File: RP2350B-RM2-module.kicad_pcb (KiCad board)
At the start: 4 copper layers, 33.7 x 68.8 mm, 58 parts, among them J1 SM03B-SRSS-TB, J2 Conn_01x26_Socket, J3 Conn_01x26_Socket, J5 USB_C_Receptacle_USB2.0_16P, SW1 SW_Push, SW2 SW_Push, U1 W25Q128JWSIQ, U2 APS6404L-SQH-SN, U3 RP2350_80QFN, U4 RM2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

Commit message: clean ERC and DRC
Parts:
- U1: value W25Q128JWSIQ -> W25Q128JVSIQ
- U2: value APS6404L-SQH-SN -> APS6404L-3SQR-SN
- U4: value RM2 -> <value>
- moved C24 0.97 mm to (91.4, 93.9)
- moved C21 0.82 mm to (91.5, 96.5)
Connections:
- net /EN renamed /3V3_EN
- U3 pad 23: +3V3 -> /WL_ON
- U4 pad 12: +3V3 -> /WL_ON
- U4 pad 13: +3V3 -> /WL_ON
- U4 pad 14: unconnected-(U4-VDDIO-Pad14) -> +3V3
- U5 pad 2: unconnected-(U5-GND-Pad2) -> GND
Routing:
- net /WL_ON: track 0.00 -> 26.0 mm, vias 0 -> 2
- net +3V3: track 55.5 -> 56.8 mm

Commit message: Changed PSRAM
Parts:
- U2: value APS6404L-3SQR-SN -> APS6404L-3SQN-SN
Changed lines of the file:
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@@
 			)
 		)
-		(property "Value" "APS6404L-3SQR-SN"
+		(property "Value" "APS6404L-3SQN-SN"
 			(at 0 3.43 0)
 			(layer "F.Fab")

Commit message: Added ADC vref
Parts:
- added C25: 100n, Capacitor_SMD:C_0402_1005Metric, F.Cu at (105.3, 70.9)
- added C26: 100n, Capacitor_SMD:C_0402_1005Metric, F.Cu at (104.3, 71.9)
- added TP2: TestPoint_Square, TestPoint:TestPoint_Pad_1.5x1.5mm, B.Cu at (109.0, 48.0)
- added TP3: TestPoint, TestPoint:TestPoint_Pad_D1.5mm, F.Cu at (102.0, 64.2)
- added U6: MCP1501-30xCH, Package_TO_SOT_SMD:SOT-23-6, F.Cu at (105.9, 68.5)
- moved C19 1.27 mm to (102.7, 70.3), turned to 90 degrees
- moved C8 0.45 mm to (102.7, 68.5)
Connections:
- U3 pad 59: +3V3 -> /ADC_AVDD
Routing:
- net /RUN: track 16.5 -> 55.8 mm, vias 3 -> 6
- net /ADC_AVDD: track 0.00 -> 15.0 mm
- net /PSRAM_CS: track 39.5 -> 47.6 mm
- net GND: track 5.63 -> 8.18 mm, vias 55 -> 57
- net +3V3: track 56.8 -> 58.3 mm, vias 21 -> 22
- net /GPIO46_ADC6: track 21.5 -> 22.9 mm
- net /GPIO42_ADC2: track 13.2 -> 14.6 mm
- net /GPIO44_ADC4: track 17.4 -> 18.7 mm
- net /GPIO45_ADC5: track 19.5 -> 20.8 mm
- net /GPIO43_ADC3: track 15.4 -> 16.6 mm
- net /GPIO41_ADC1: track 12.3 -> 12.9 mm
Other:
- board text added: "1"
- board text added: "IAN ARCHBELL"
- board text added: "MIT LIC."

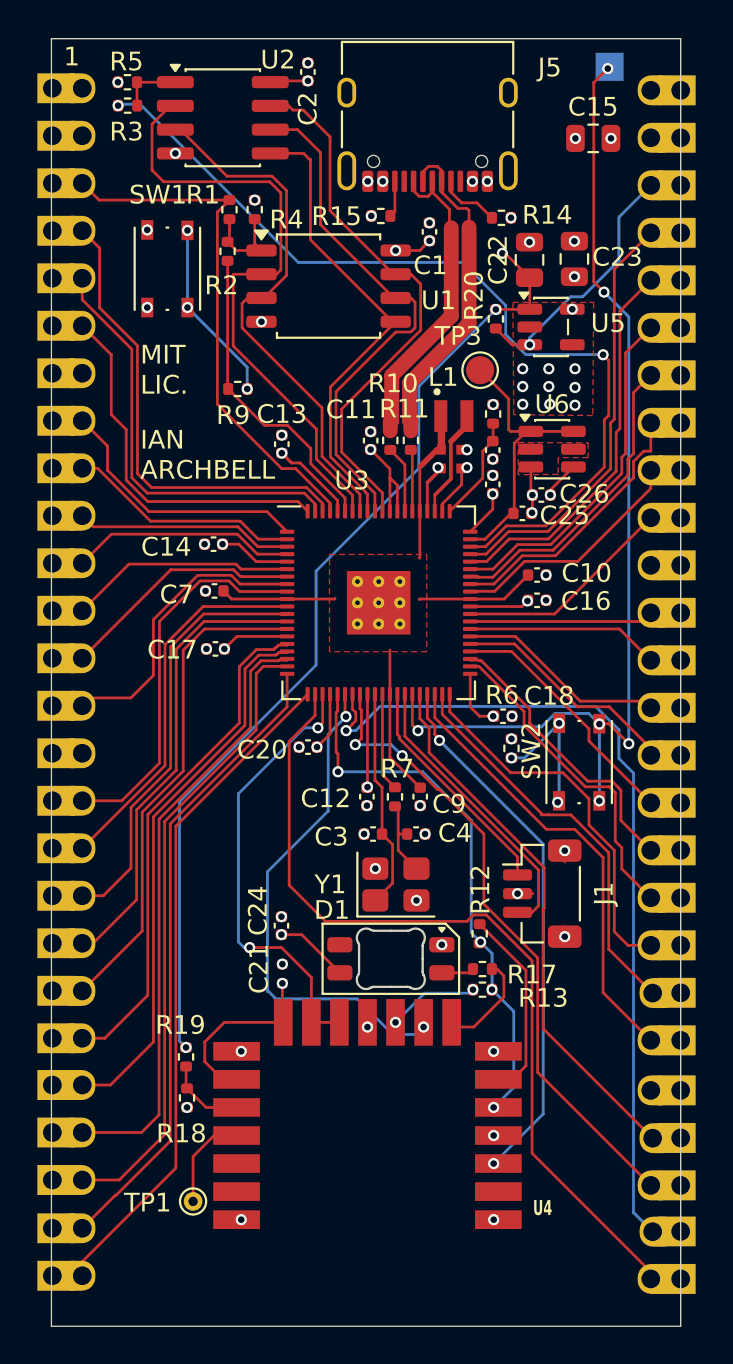
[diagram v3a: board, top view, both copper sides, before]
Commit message: Added pin numbering
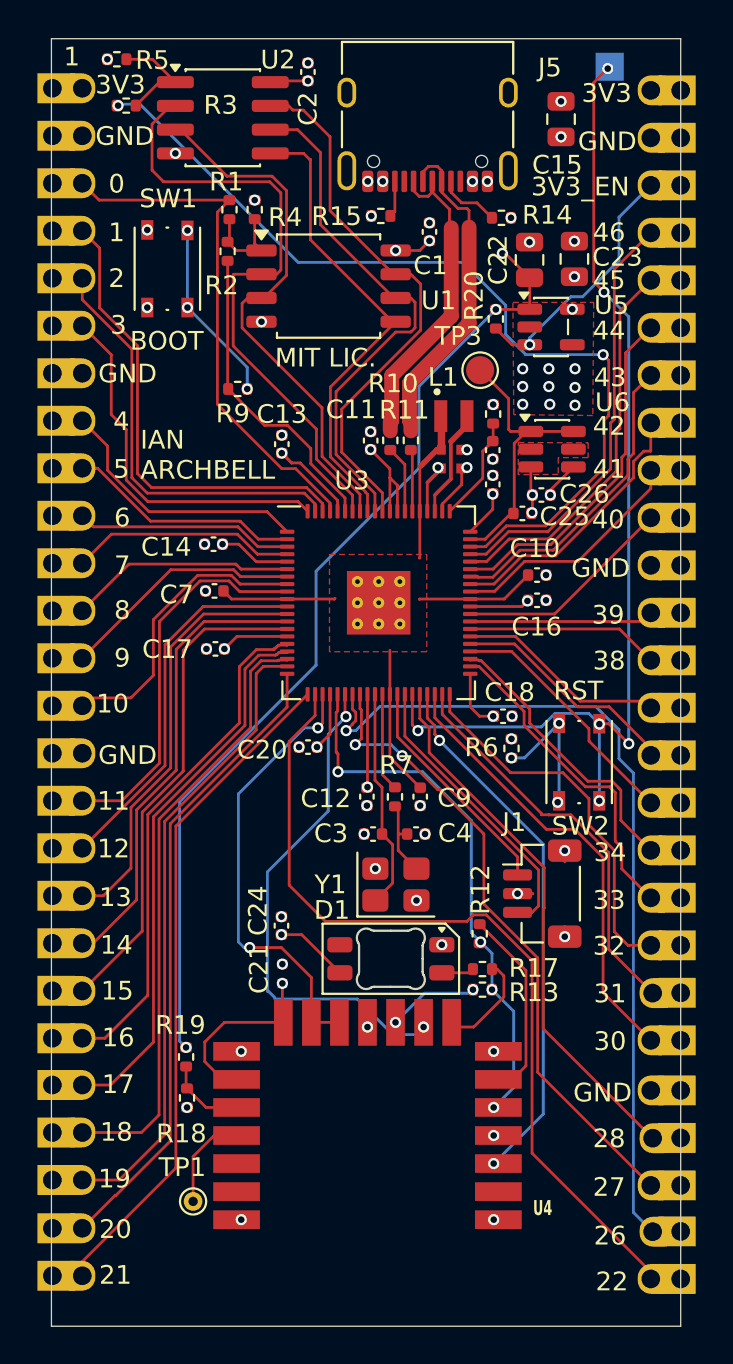
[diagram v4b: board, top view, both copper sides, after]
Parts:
- moved C15 2.00 mm to (106.3, 50.8), turned to -90 degrees
- moved R5 1.35 mm to (82.6, 47.6)
- moved R3 0.08 mm to (83.1, 50.1)
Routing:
- net /FLASH2_SS: track 3.31 -> 5.76 mm
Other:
- board text added: "0"
- board text added: "10"
- board text added: "11"
- board text added: "12"
- board text added: "13"
- board text added: "14"
- board text added: "15"
- board text added: "16"
- board text added: "17"
- board text added: "18"
- board text added: "19"
- board text added: "2"
- board text added: "20"
- board text added: "21"
- board text added: "22"
- board text added: "26"
- board text added: "27"
- board text added: "28"
- board text added: "3"
- board text added: "30"
- board text added: "31"
- board text added: "32"
- board text added: "33"
- board text added: "34"
- board text added: "38"
- board text added: "39"
- board text added: "3V3"
- board text added: "3V3_EN"
- board text added: "4"
- board text added: "40"
- board text added: "41"
- board text added: "42"
- board text added: "43"
- board text added: "44"
- board text added: "45"
- board text added: "46"
- board text added: "5"
- board text added: "6"
- board text added: "7"
- board text added: "8"
- board text added: "9"
- board text added: "BOOT"
- board text added: "GND"
- board text added: "RST"

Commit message: Added pin numbering
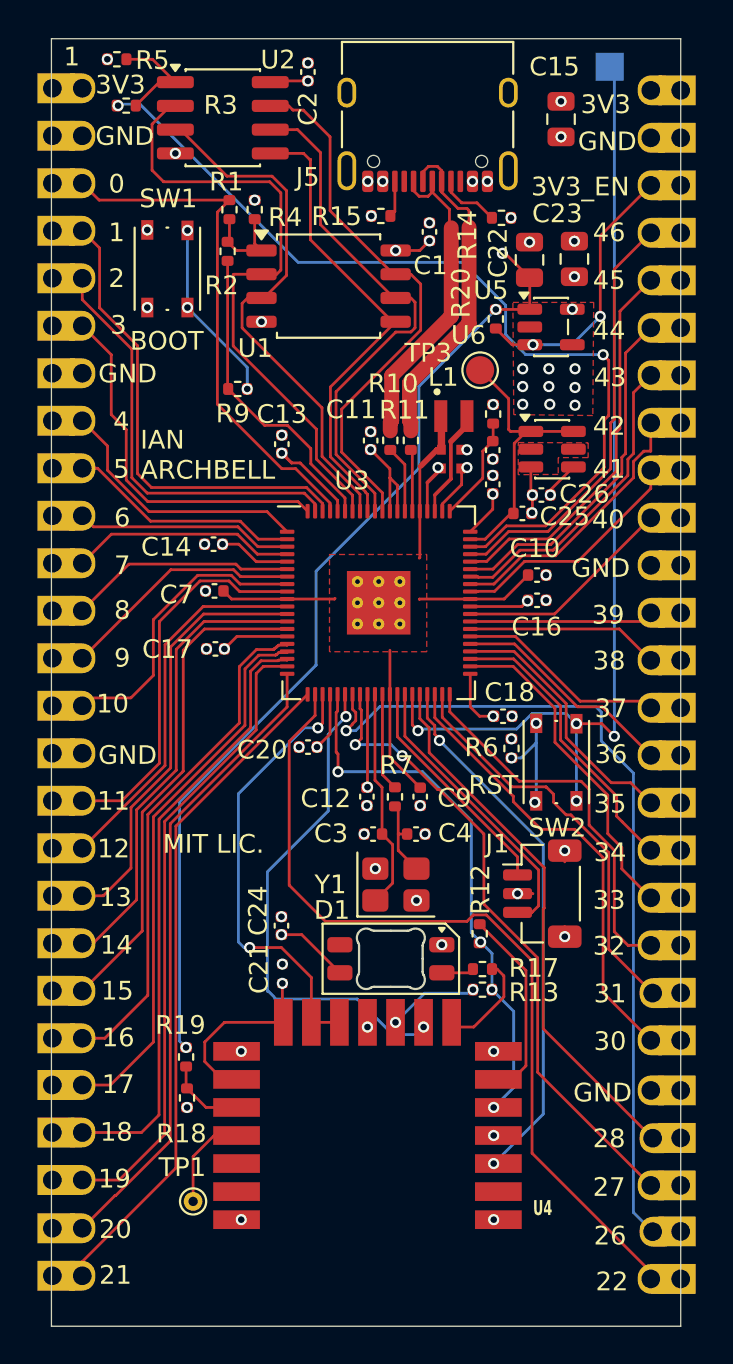
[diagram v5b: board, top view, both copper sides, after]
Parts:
- moved SW2 1.22 mm to (106.1, 85.2)
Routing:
- net /RUN: track 55.8 -> 53.5 mm, vias 6 -> 4
- net Net-(R6-Pad1): track 7.68 -> 6.02 mm
- net /3V3_EN: track 13.7 -> 15.2 mm, vias 1 -> 2
- net /GPIO35: track 13.4 -> 14.1 mm
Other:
- board text added: "35"
- board text added: "36"
- board text added: "37"
- board text added: "RUN"
